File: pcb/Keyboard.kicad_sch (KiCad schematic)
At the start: 63 parts

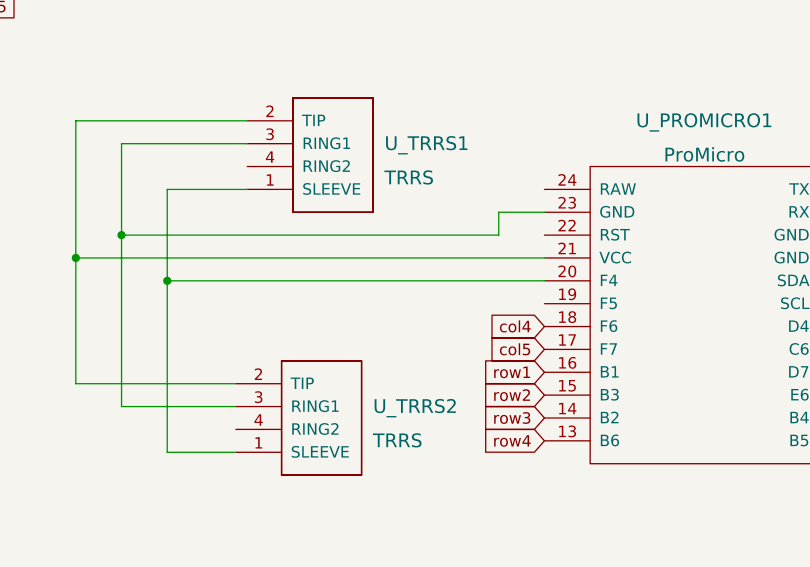
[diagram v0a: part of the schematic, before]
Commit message: Add note about wrong serial pin.
Wired this wrong. Needs to go to D0, D1, D2, D3, or E6.
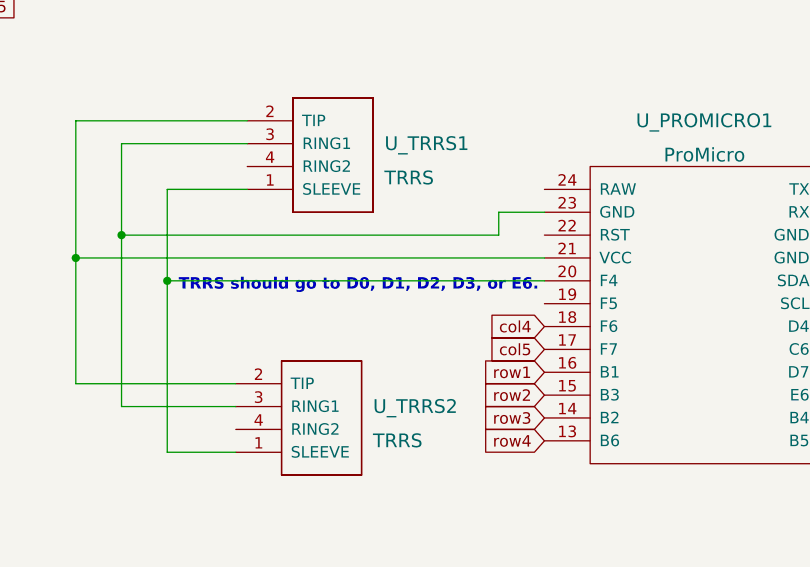
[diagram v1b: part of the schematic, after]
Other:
- note added: "TRRS should go to D0, D1, D2, D3, or E6."
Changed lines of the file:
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@@
     (stroke (width 0) (type default) (color 0 0 0 0))
+  )
+  (text "TRRS should go to D0, D1, D2, D3, or E6." (at 186.69 54.61 0)
+    (effects (font (size 1.27 1.27) (thickness 0.254) bold) (justify left bottom))
   )
   (global_label "col5" (shape input) (at 227.33 60.96 180) (fields_autoplaced)

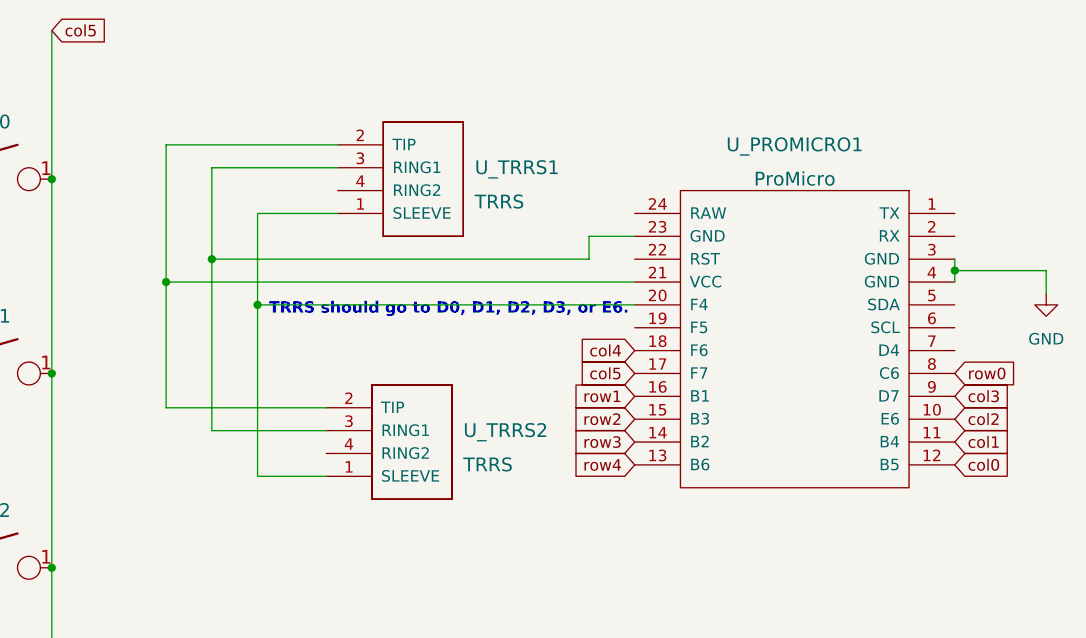
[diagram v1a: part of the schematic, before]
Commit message: Fix TRRS jack wiring.
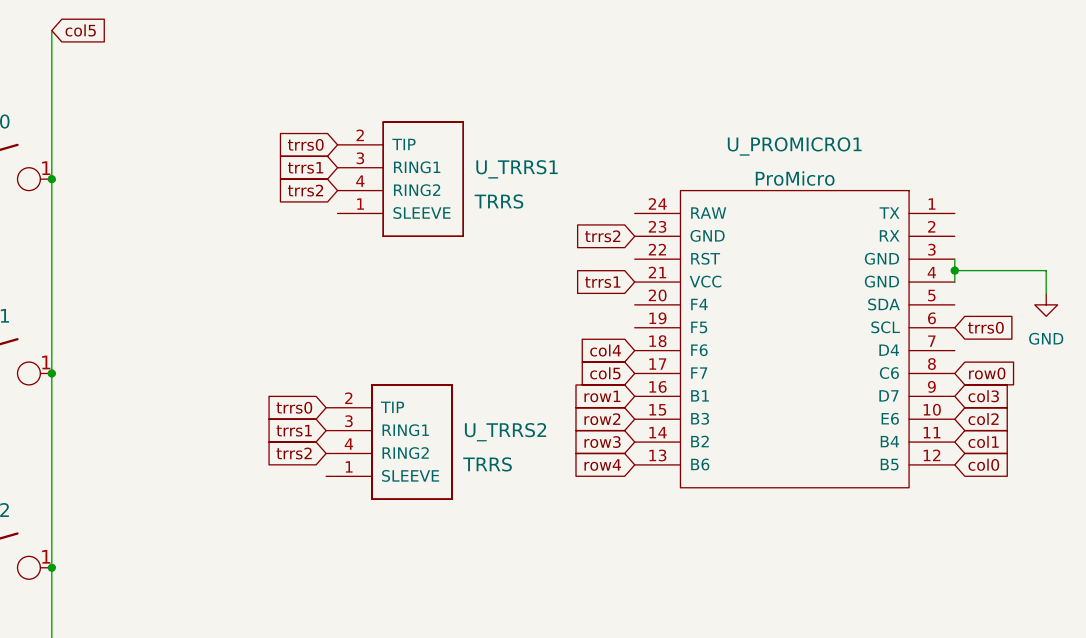
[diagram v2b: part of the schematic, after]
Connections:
- net trrs0: now reaches U_TRRS1.2 (TIP), U_TRRS2.2 (TIP)
- net trrs0: now also U_PROMICRO1.6 (SCL); no longer U_PROMICRO1.21 (VCC)
- net trrs1: now reaches U_TRRS1.3 (RING1), U_TRRS2.3 (RING1)
- net trrs1: now also U_PROMICRO1.21 (VCC); no longer U_PROMICRO1.23 (GND)
- net trrs2: now reaches U_TRRS1.4 (RING2)
- net trrs2: now also U_PROMICRO1.23 (GND), U_TRRS2.4 (RING2)
- now unconnected: U_PROMICRO1.20 (F4), U_TRRS1.1 (SLEEVE), U_TRRS2.1 (SLEEVE)
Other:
- note removed: "TRRS should go to D0, D1, D2, D3, or E6."
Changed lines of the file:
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@@
   (junction (at 26.67 49.53) (diameter 0) (color 0 0 0 0)
   )
-  (junction (at 185.42 53.34) (diameter 0) (color 0 0 0 0)
-  )
   (junction (at 90.17 39.37) (diameter 0) (color 0 0 0 0)
   )
@@
   (junction (at 123.19 135.89) (diameter 0) (color 0 0 0 0)
   )
-  (junction (at 175.26 50.8) (diameter 0) (color 0 0 0 0)
-  )
   (junction (at 90.17 60.96) (diameter 0) (color 0 0 0 0)
   )
@@
   (junction (at 114.3 82.55) (diameter 0) (color 0 0 0 0)
   )
-  (junction (at 180.34 48.26) (diameter 0) (color 0 0 0 0)
-  )
   (junction (at 90.17 82.55) (diameter 0) (color 0 0 0 0)
   )
@@
     (stroke (width 0) (type default) (color 0 0 0 0))
   )
-  (wire (pts (xy 175.26 50.8) (xy 175.26 64.77))
-    (stroke (width 0) (type default) (color 0 0 0 0))
-  )
   (wire (pts (xy 26.67 148.59) (xy 22.86 148.59))
     (stroke (width 0) (type default) (color 0 0 0 0))
@@
     (stroke (width 0) (type default) (color 0 0 0 0))
   )
-  (wire (pts (xy 222.25 45.72) (xy 227.33 45.72))
-    (stroke (width 0) (type default) (color 0 0 0 0))
-  )
   (wire (pts (xy 123.19 114.3) (xy 147.32 114.3))
     (stroke (width 0) (type default) (color 0 0 0 0))
@@
     (stroke (width 0) (type default) (color 0 0 0 0))
   )
-  (wire (pts (xy 185.42 53.34) (xy 185.42 72.39))
-    (stroke (width 0) (type default) (color 0 0 0 0))
-  )
   (wire (pts (xy 66.04 60.96) (xy 66.04 82.55))
     (stroke (width 0) (type default) (color 0 0 0 0))
@@
     (stroke (width 0) (type default) (color 0 0 0 0))
   )
-  (wire (pts (xy 185.42 43.18) (xy 194.31 43.18))
-    (stroke (width 0) (type default) (color 0 0 0 0))
-  )
   (wire (pts (xy 262.89 49.53) (xy 262.89 50.8))
     (stroke (width 0) (type default) (color 0 0 0 0))
   )
-  (wire (pts (xy 180.34 38.1) (xy 180.34 48.26))
-    (stroke (width 0) (type default) (color 0 0 0 0))
-  )
   (wire (pts (xy 162.56 22.86) (xy 162.56 39.37))
     (stroke (width 0) (type default) (color 0 0 0 0))
@@
     (stroke (width 0) (type default) (color 0 0 0 0))
   )
-  (wire (pts (xy 222.25 48.26) (xy 222.25 45.72))
-    (stroke (width 0) (type default) (color 0 0 0 0))
-  )
   (wire (pts (xy 147.32 82.55) (xy 147.32 85.09))
     (stroke (width 0) (type default) (color 0 0 0 0))
@@
     (stroke (width 0) (type default) (color 0 0 0 0))
   )
-  (wire (pts (xy 193.04 67.31) (xy 180.34 67.31))
-    (stroke (width 0) (type default) (color 0 0 0 0))
-  )
   (wire (pts (xy 147.32 104.14) (xy 147.32 106.68))
     (stroke (width 0) (type default) (color 0 0 0 0))
@@
     (stroke (width 0) (type default) (color 0 0 0 0))
   )
-  (wire (pts (xy 175.26 35.56) (xy 175.26 50.8))
-    (stroke (width 0) (type default) (color 0 0 0 0))
-  )
-  (wire (pts (xy 175.26 50.8) (xy 227.33 50.8))
-    (stroke (width 0) (type default) (color 0 0 0 0))
-  )
   (wire (pts (xy 26.67 104.14) (xy 26.67 106.68))
     (stroke (width 0) (type default) (color 0 0 0 0))
@@
     (stroke (width 0) (type default) (color 0 0 0 0))
   )
-  (wire (pts (xy 194.31 35.56) (xy 175.26 35.56))
-    (stroke (width 0) (type default) (color 0 0 0 0))
-  )
   (wire (pts (xy 90.17 60.96) (xy 90.17 82.55))
     (stroke (width 0) (type default) (color 0 0 0 0))
@@
     (stroke (width 0) (type default) (color 0 0 0 0))
   )
-  (wire (pts (xy 185.42 43.18) (xy 185.42 53.34))
-    (stroke (width 0) (type default) (color 0 0 0 0))
-  )
-  (wire (pts (xy 193.04 64.77) (xy 175.26 64.77))
-    (stroke (width 0) (type default) (color 0 0 0 0))
-  )
   (wire (pts (xy 26.67 125.73) (xy 26.67 128.27))
     (stroke (width 0) (type default) (color 0 0 0 0))
   )
-  (wire (pts (xy 180.34 48.26) (xy 222.25 48.26))
-    (stroke (width 0) (type default) (color 0 0 0 0))
-  )
   (wire (pts (xy 99.06 148.59) (xy 95.25 148.59))
     (stroke (width 0) (type default) (color 0 0 0 0))
@@
     (stroke (width 0) (type default) (color 0 0 0 0))
   )
-  (wire (pts (xy 193.04 72.39) (xy 185.42 72.39))
-    (stroke (width 0) (type default) (color 0 0 0 0))
-  )
   (wire (pts (xy 50.8 71.12) (xy 74.93 71.12))
     (stroke (width 0) (type default) (color 0 0 0 0))
@@
     (stroke (width 0) (type default) (color 0 0 0 0))
   )
-  (wire (pts (xy 180.34 67.31) (xy 180.34 48.26))
-    (stroke (width 0) (type default) (color 0 0 0 0))
-  )
   (wire (pts (xy 20.32 71.12) (xy 26.67 71.12))
     (stroke (width 0) (type default) (color 0 0 0 0))
@@
     (stroke (width 0) (type default) (color 0 0 0 0))
   )
-  (wire (pts (xy 185.42 53.34) (xy 227.33 53.34))
-    (stroke (width 0) (type default) (color 0 0 0 0))
-  )
   (wire (pts (xy 114.3 39.37) (xy 114.3 60.96))
     (stroke (width 0) (type default) (color 0 0 0 0))
@@
     (stroke (width 0) (type default) (color 0 0 0 0))
   )
-  (wire (pts (xy 194.31 38.1) (xy 180.34 38.1))
-    (stroke (width 0) (type default) (color 0 0 0 0))
-  )
-  (text "TRRS should go to D0, D1, D2, D3, or E6." (at 186.69 54.61 0)
-    (effects (font (size 1.27 1.27) (thickness 0.254) bold) (justify left bottom))
-  )
   (global_label "col5" (shape input) (at 227.33 60.96 180) (fields_autoplaced)
     (effects (font (size 1.27 1.27)) (justify right))
@@
     )
   )
+  (global_label "trrs0" (shape input) (at 194.31 35.56 180) (fields_autoplaced)
+    (effects (font (size 1.27 1.27)) (justify right))
+    (property "Intersheet References" "${INTERSHEET_REFS}" (id 0) (at 187.3612 35.4806 0)
+      (effects (font (size 1.27 1.27)) (justify right) hide)
+    )
+  )
   (global_label "col4" (shape input) (at 138.43 22.86 0) (fields_autoplaced)
     (effects (font (size 1.27 1.27)) (justify left))
@@
     )
   )
+  (global_label "trrs0" (shape input) (at 262.89 55.88 0) (fields_autoplaced)
+    (effects (font (size 1.27 1.27)) (justify left))
+    (property "Intersheet References" "${INTERSHEET_REFS}" (id 0) (at 269.8388 55.8006 0)
+      (effects (font (size 1.27 1.27)) (justify left) hide)
+    )
+  )
+  (global_label "trrs2" (shape input) (at 193.04 69.85 180) (fields_autoplaced)
+    (effects (font (size 1.27 1.27)) (justify right))
+    (property "Intersheet References" "${INTERSHEET_REFS}" (id 0) (at 186.0912 69.7706 0)
+      (effects (font (size 1.27 1.27)) (justify right) hide)
+    )
+  )
   (global_label "col1" (shape input) (at 66.04 22.86 0) (fields_autoplaced)
     (effects (font (size 1.27 1.27)) (justify left))
@@
     )
   )
+  (global_label "trrs1" (shape input) (at 227.33 50.8 180) (fields_autoplaced)
+    (effects (font (size 1.27 1.27)) (justify right))
+    (property "Intersheet References" "${INTERSHEET_REFS}" (id 0) (at 220.3812 50.7206 0)
+      (effects (font (size 1.27 1.27)) (justify right) hide)
+    )
+  )
   (global_label "row4" (shape input) (at 20.32 135.89 180) (fields_autoplaced)
     (effects (font (size 1.27 1.27)) (justify right))
@@
     )
   )
+  (global_label "trrs1" (shape input) (at 193.04 67.31 180) (fields_autoplaced)
+    (effects (font (size 1.27 1.27)) (justify right))
+    (property "Intersheet References" "${INTERSHEET_REFS}" (id 0) (at 186.0912 67.2306 0)
+      (effects (font (size 1.27 1.27)) (justify right) hide)
+    )
+  )
+  (global_label "trrs2" (shape input) (at 227.33 45.72 180) (fields_autoplaced)
+    (effects (font (size 1.27 1.27)) (justify right))
+    (property "Intersheet References" "${INTERSHEET_REFS}" (id 0) (at 220.3812 45.6406 0)
+      (effects (font (size 1.27 1.27)) (justify right) hide)
+    )
+  )
+  (global_label "trrs2" (shape input) (at 194.31 40.64 180) (fields_autoplaced)
+    (effects (font (size 1.27 1.27)) (justify right))
+    (property "Intersheet References" "${INTERSHEET_REFS}" (id 0) (at 187.3612 40.5606 0)
+      (effects (font (size 1.27 1.27)) (justify right) hide)
+    )
+  )
   (global_label "row1" (shape input) (at 20.32 71.12 180) (fields_autoplaced)
     (effects (font (size 1.27 1.27)) (justify right))
@@
     )
   )
+  (global_label "trrs0" (shape input) (at 193.04 64.77 180) (fields_autoplaced)
+    (effects (font (size 1.27 1.27)) (justify right))
+    (property "Intersheet References" "${INTERSHEET_REFS}" (id 0) (at 186.0912 64.6906 0)
+      (effects (font (size 1.27 1.27)) (justify right) hide)
+    )
+  )
   (global_label "row1" (shape input) (at 227.33 63.5 180) (fields_autoplaced)
     (effects (font (size 1.27 1.27)) (justify right))
@@
     )
   )
+  (global_label "trrs1" (shape input) (at 194.31 38.1 180) (fields_autoplaced)
+    (effects (font (size 1.27 1.27)) (justify right))
+    (property "Intersheet References" "${INTERSHEET_REFS}" (id 0) (at 187.3612 38.0206 0)
+      (effects (font (size 1.27 1.27)) (justify right) hide)
+    )
+  )

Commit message: wip
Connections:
- net GND: now also U_PROMICRO1.23 (GND), U_TRRS1.3 (RING1), U_TRRS2.3 (RING1)
- net trrs0 renamed trrs
- removed net trrs1: U_PROMICRO1.21 (VCC), U_TRRS1.3 (RING1), U_TRRS2.3 (RING1)
- net trrs2 renamed VCC
- net VCC: now also U_PROMICRO1.21 (VCC); no longer U_PROMICRO1.23 (GND)
- no-connect marks 0 -> 10

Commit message: wip
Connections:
- net col0: now also U_PROMICRO1.7 (D4); no longer U_PROMICRO1.12 (B5)
- net col1: now also U_PROMICRO1.8 (C6); no longer U_PROMICRO1.11 (B4)
- net col2: now also U_PROMICRO1.9 (D7); no longer U_PROMICRO1.10 (E6)
- net col3: now also U_PROMICRO1.10 (E6); no longer U_PROMICRO1.9 (D7)
- net col4: now also U_PROMICRO1.11 (B4); no longer U_PROMICRO1.18 (F6)
- net col5: now also U_PROMICRO1.12 (B5); no longer U_PROMICRO1.17 (F7)
- net row0: now also U_PROMICRO1.17 (F7); no longer U_PROMICRO1.8 (C6)
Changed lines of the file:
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@@
   (no_connect (at 262.89 45.72))
   (no_connect (at 262.89 43.18))
-  (no_connect (at 262.89 58.42))
+  (no_connect (at 227.33 58.42))
   (no_connect (at 193.04 72.39))
   (no_connect (at 194.31 43.18))
@@
     (stroke (width 0) (type default) (color 0 0 0 0))
   )
-  (global_label "col5" (shape input) (at 227.33 60.96 180) (fields_autoplaced)
-    (effects (font (size 1.27 1.27)) (justify right))
-    (property "Intersheet References" "${INTERSHEET_REFS}" (id 0) (at 220.8045 60.8806 0)
-      (effects (font (size 1.27 1.27)) (justify right) hide)
-    )
-  )
-  (global_label "col3" (shape input) (at 262.89 63.5 0) (fields_autoplaced)
+  (global_label "col5" (shape input) (at 262.89 71.12 0) (fields_autoplaced)
+    (effects (font (size 1.27 1.27)) (justify left))
+    (property "Intersheet References" "${INTERSHEET_REFS}" (id 0) (at 269.4155 71.0406 0)
+      (effects (font (size 1.27 1.27)) (justify left) hide)
+    )
+  )
+  (global_label "col3" (shape input) (at 262.89 66.04 0) (fields_autoplaced)
+    (effects (font (size 1.27 1.27)) (justify left))
+    (property "Intersheet References" "${INTERSHEET_REFS}" (id 0) (at 269.4155 65.9606 0)
+      (effects (font (size 1.27 1.27)) (justify left) hide)
+    )
+  )
+  (global_label "row4" (shape input) (at 227.33 71.12 180) (fields_autoplaced)
+    (effects (font (size 1.27 1.27)) (justify right))
+    (property "Intersheet References" "${INTERSHEET_REFS}" (id 0) (at 220.4417 71.0406 0)
+      (effects (font (size 1.27 1.27)) (justify right) hide)
+    )
+  )
+  (global_label "trrs" (shape input) (at 194.31 35.56 180) (fields_autoplaced)
+    (effects (font (size 1.27 1.27)) (justify right))
+    (property "Intersheet References" "${INTERSHEET_REFS}" (id 0) (at 188.5707 35.4806 0)
+      (effects (font (size 1.27 1.27)) (justify right) hide)
+    )
+  )
+  (global_label "col4" (shape input) (at 138.43 22.86 0) (fields_autoplaced)
+    (effects (font (size 1.27 1.27)) (justify left))
+    (property "Intersheet References" "${INTERSHEET_REFS}" (id 0) (at 144.9555 22.7806 0)
+      (effects (font (size 1.27 1.27)) (justify left) hide)
+    )
+  )
+  (global_label "row2" (shape input) (at 227.33 66.04 180) (fields_autoplaced)
+    (effects (font (size 1.27 1.27)) (justify right))
+    (property "Intersheet References" "${INTERSHEET_REFS}" (id 0) (at 220.4417 65.9606 0)
+      (effects (font (size 1.27 1.27)) (justify right) hide)
+    )
+  )
+  (global_label "trrs" (shape input) (at 262.89 55.88 0) (fields_autoplaced)
+    (effects (font (size 1.27 1.27)) (justify left))
+    (property "Intersheet References" "${INTERSHEET_REFS}" (id 0) (at 268.6293 55.8006 0)
+      (effects (font (size 1.27 1.27)) (justify left) hide)
+    )
+  )
+  (global_label "col1" (shape input) (at 66.04 22.86 0) (fields_autoplaced)
+    (effects (font (size 1.27 1.27)) (justify left))
+    (property "Intersheet References" "${INTERSHEET_REFS}" (id 0) (at 72.5655 22.7806 0)
+      (effects (font (size 1.27 1.27)) (justify left) hide)
+    )
+  )
+  (global_label "col2" (shape input) (at 262.89 63.5 0) (fields_autoplaced)
     (effects (font (size 1.27 1.27)) (justify left))
     (property "Intersheet References" "${INTERSHEET_REFS}" (id 0) (at 269.4155 63.4206 0)
@@
     )
   )
-  (global_label "row4" (shape input) (at 227.33 71.12 180) (fields_autoplaced)
-    (effects (font (size 1.27 1.27)) (justify right))
-    (property "Intersheet References" "${INTERSHEET_REFS}" (id 0) (at 220.4417 71.0406 0)
-      (effects (font (size 1.27 1.27)) (justify right) hide)
-    )
-  )
-  (global_label "trrs" (shape input) (at 194.31 35.56 180) (fields_autoplaced)
-    (effects (font (size 1.27 1.27)) (justify right))
-    (property "Intersheet References" "${INTERSHEET_REFS}" (id 0) (at 188.5707 35.4806 0)
-      (effects (font (size 1.27 1.27)) (justify right) hide)
-    )
-  )
-  (global_label "col4" (shape input) (at 138.43 22.86 0) (fields_autoplaced)
-    (effects (font (size 1.27 1.27)) (justify left))
-    (property "Intersheet References" "${INTERSHEET_REFS}" (id 0) (at 144.9555 22.7806 0)
-      (effects (font (size 1.27 1.27)) (justify left) hide)
-    )
-  )
-  (global_label "row2" (shape input) (at 227.33 66.04 180) (fields_autoplaced)
-    (effects (font (size 1.27 1.27)) (justify right))
-    (property "Intersheet References" "${INTERSHEET_REFS}" (id 0) (at 220.4417 65.9606 0)
-      (effects (font (size 1.27 1.27)) (justify right) hide)
-    )
-  )
-  (global_label "trrs" (shape input) (at 262.89 55.88 0) (fields_autoplaced)
-    (effects (font (size 1.27 1.27)) (justify left))
-    (property "Intersheet References" "${INTERSHEET_REFS}" (id 0) (at 268.6293 55.8006 0)
-      (effects (font (size 1.27 1.27)) (justify left) hide)
-    )
-  )
-  (global_label "col1" (shape input) (at 66.04 22.86 0) (fields_autoplaced)
-    (effects (font (size 1.27 1.27)) (justify left))
-    (property "Intersheet References" "${INTERSHEET_REFS}" (id 0) (at 72.5655 22.7806 0)
-      (effects (font (size 1.27 1.27)) (justify left) hide)
-    )
-  )
-  (global_label "col2" (shape input) (at 262.89 66.04 0) (fields_autoplaced)
-    (effects (font (size 1.27 1.27)) (justify left))
-    (property "Intersheet References" "${INTERSHEET_REFS}" (id 0) (at 269.4155 65.9606 0)
-      (effects (font (size 1.27 1.27)) (justify left) hide)
-    )
-  )
   (global_label "col3" (shape input) (at 114.3 22.86 0) (fields_autoplaced)
     (effects (font (size 1.27 1.27)) (justify left))
@@
     )
   )
-  (global_label "col4" (shape input) (at 227.33 58.42 180) (fields_autoplaced)
-    (effects (font (size 1.27 1.27)) (justify right))
-    (property "Intersheet References" "${INTERSHEET_REFS}" (id 0) (at 220.8045 58.3406 0)
-      (effects (font (size 1.27 1.27)) (justify right) hide)
+  (global_label "col4" (shape input) (at 262.89 68.58 0) (fields_autoplaced)
+    (effects (font (size 1.27 1.27)) (justify left))
+    (property "Intersheet References" "${INTERSHEET_REFS}" (id 0) (at 269.4155 68.5006 0)
+      (effects (font (size 1.27 1.27)) (justify left) hide)
     )
   )
@@
     )
   )
-  (global_label "row0" (shape input) (at 262.89 60.96 0) (fields_autoplaced)
-    (effects (font (size 1.27 1.27)) (justify left))
-    (property "Intersheet References" "${INTERSHEET_REFS}" (id 0) (at 269.7783 60.8806 0)
-      (effects (font (size 1.27 1.27)) (justify left) hide)
+  (global_label "row0" (shape input) (at 227.33 60.96 180) (fields_autoplaced)
+    (effects (font (size 1.27 1.27)) (justify right))
+    (property "Intersheet References" "${INTERSHEET_REFS}" (id 0) (at 220.4417 60.8806 0)
+      (effects (font (size 1.27 1.27)) (justify right) hide)
     )
   )
@@
     )
   )
-  (global_label "col0" (shape input) (at 262.89 71.12 0) (fields_autoplaced)
-    (effects (font (size 1.27 1.27)) (justify left))
-    (property "Intersheet References" "${INTERSHEET_REFS}" (id 0) (at 269.4155 71.0406 0)
+  (global_label "col0" (shape input) (at 262.89 58.42 0) (fields_autoplaced)
+    (effects (font (size 1.27 1.27)) (justify left))
+    (property "Intersheet References" "${INTERSHEET_REFS}" (id 0) (at 269.4155 58.3406 0)
       (effects (font (size 1.27 1.27)) (justify left) hide)
     )
@@
     )
   )
-  (global_label "col1" (shape input) (at 262.89 68.58 0) (fields_autoplaced)
-    (effects (font (size 1.27 1.27)) (justify left))
-    (property "Intersheet References" "${INTERSHEET_REFS}" (id 0) (at 269.4155 68.5006 0)
-      (effects (font (size 1.27 1.27)) (justify left) hide)
-    )
+  (global_label "col1" (shape input) (at 262.89 60.96 0) (fields_autoplaced)
+    (effects (font (size 1.27 1.27)) (justify left))
+    (property "Intersheet References" "${INTERSHEET_REFS}" (id 0) (at 269.4155 60.8806 0)
+      (effects (font (size 1.27 1.27)) (justify left) hide)
+    )
